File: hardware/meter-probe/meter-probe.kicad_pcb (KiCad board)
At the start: 2 copper layers, 38.9 x 74.1 mm, 19 parts, among them J1 Main Board, Q1 BSS138, SW1 Sensor Button, U1 RT9193, U2 TCS3472, U3 P82B96

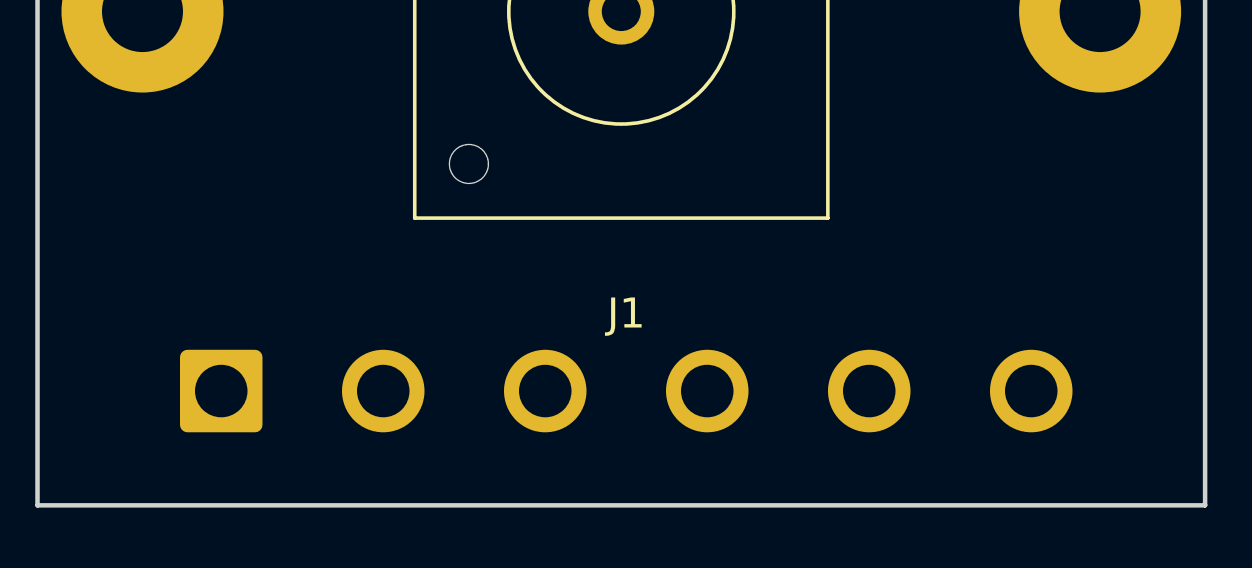
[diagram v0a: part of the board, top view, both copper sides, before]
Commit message: Updated wire connection footprint and PCB labeling
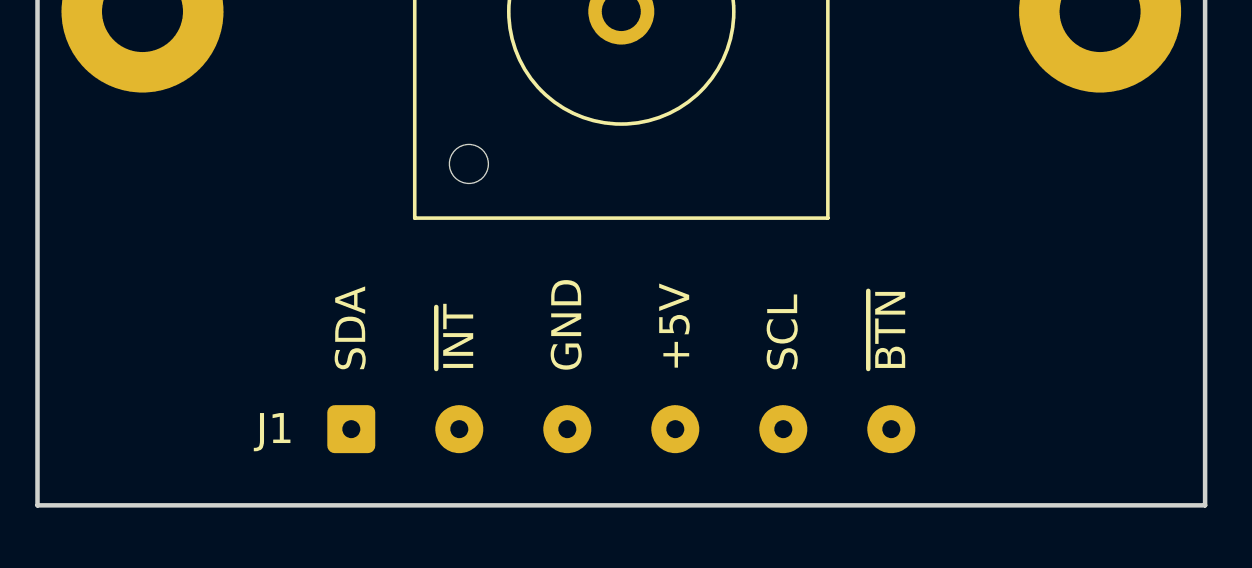
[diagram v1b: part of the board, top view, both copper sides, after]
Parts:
- J1: footprint Connector_Wire:SolderWire-1sqmm_1x06_P5.4mm_D1.4mm_OD2.7mm -> Connector_Wire:SolderWire-0.1sqmm_1x06_P3.6mm_D0.4mm_OD1mm
- moved J1 4.52 mm to (111.7, 130.8)
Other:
- board text added: "+5V"
- board text added: "GND"
- board text added: "SCL"
- board text added: "SDA"
- board text added: "~BTN"
- board text added: "~INT"

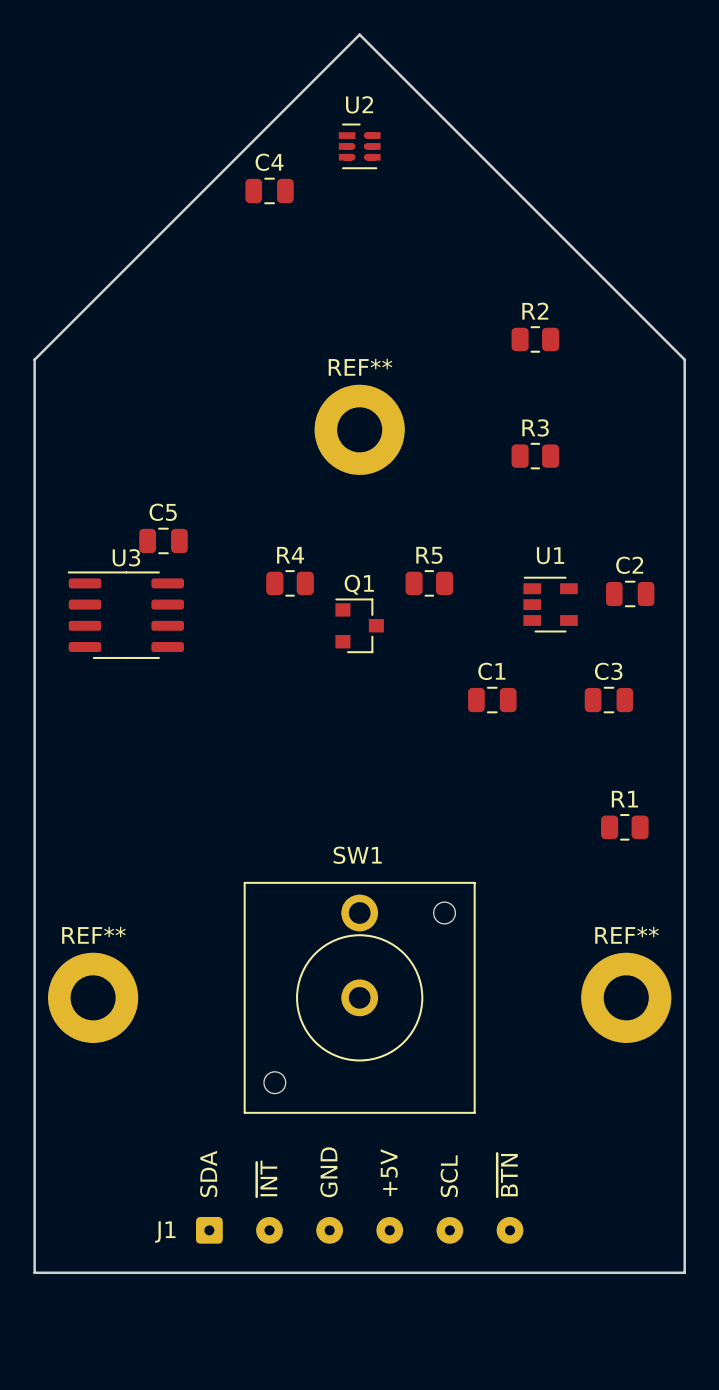
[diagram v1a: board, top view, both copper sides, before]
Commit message: Initial meter probe PCB layout
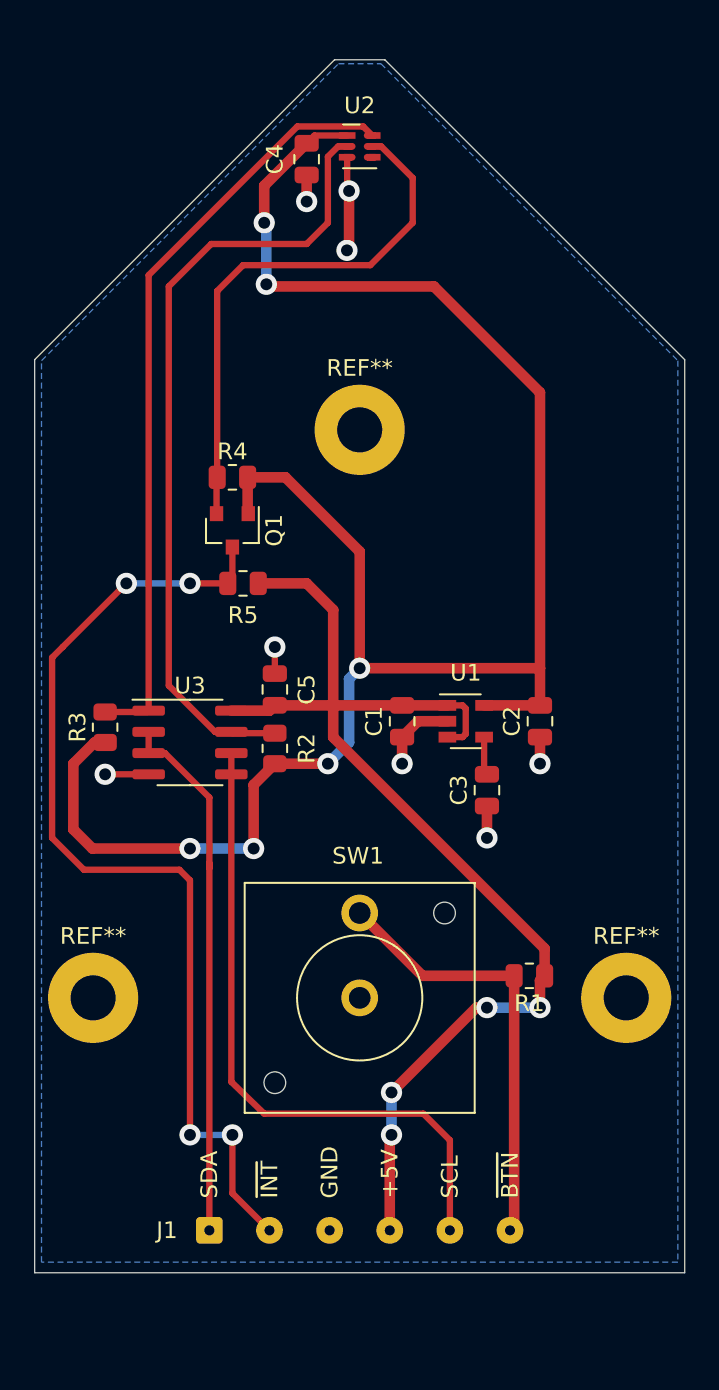
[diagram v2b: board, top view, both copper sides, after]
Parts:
- moved R3 30.4 mm to (105.4, 100.7), turned to 90 degrees
- moved R2 29.0 mm to (115.6, 102.0), turned to 90 degrees
- moved R5 11.2 mm to (113.7, 92.1), turned to 180 degrees
- moved C5 11.1 mm to (115.6, 98.4), turned to 90 degrees
- moved R1 10.6 mm to (130.8, 115.6), turned to 180 degrees
- moved Q1 9.52 mm to (113.0, 88.9), turned to 270 degrees
- moved C2 9.34 mm to (131.4, 100.3), turned to 90 degrees
- moved C3 9.08 mm to (128.3, 104.5), turned to 90 degrees
- moved U1 8.64 mm to (127.0, 100.3)
- moved U3 8.52 mm to (110.5, 101.6)
- moved R4 7.23 mm to (113.0, 85.7), turned to 180 degrees
- moved C1 5.55 mm to (123.2, 100.3), turned to 90 degrees
- moved C4 2.93 mm to (117.5, 66.7), turned to 270 degrees
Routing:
- net +3V3: track 0.00 -> 114.8 mm, vias 0 -> 6
- net +5V: track 0.00 -> 70.6 mm, vias 0 -> 4
- net /~INT: track 0.00 -> 59.2 mm, vias 0 -> 4
- net Net-(R2-Pad2): track 0.00 -> 47.9 mm
- net Net-(R3-Pad2): track 0.00 -> 46.0 mm
- net /SCL: track 0.00 -> 39.6 mm
- net Net-(Q1-Pad2): track 0.00 -> 32.6 mm
- net /SDA: track 0.00 -> 32.2 mm
- net /~BUTTON: track 0.00 -> 26.1 mm
- net GND: track 0.00 -> 19.7 mm, vias 0 -> 8
- net Net-(C3-Pad2): track 0.00 -> 2.30 mm
- added copper zone on B.Cu, net GND
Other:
- board size 38.9 x 74.1 mm -> 38.9 x 72.6 mm

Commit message: Updated PCB page properties
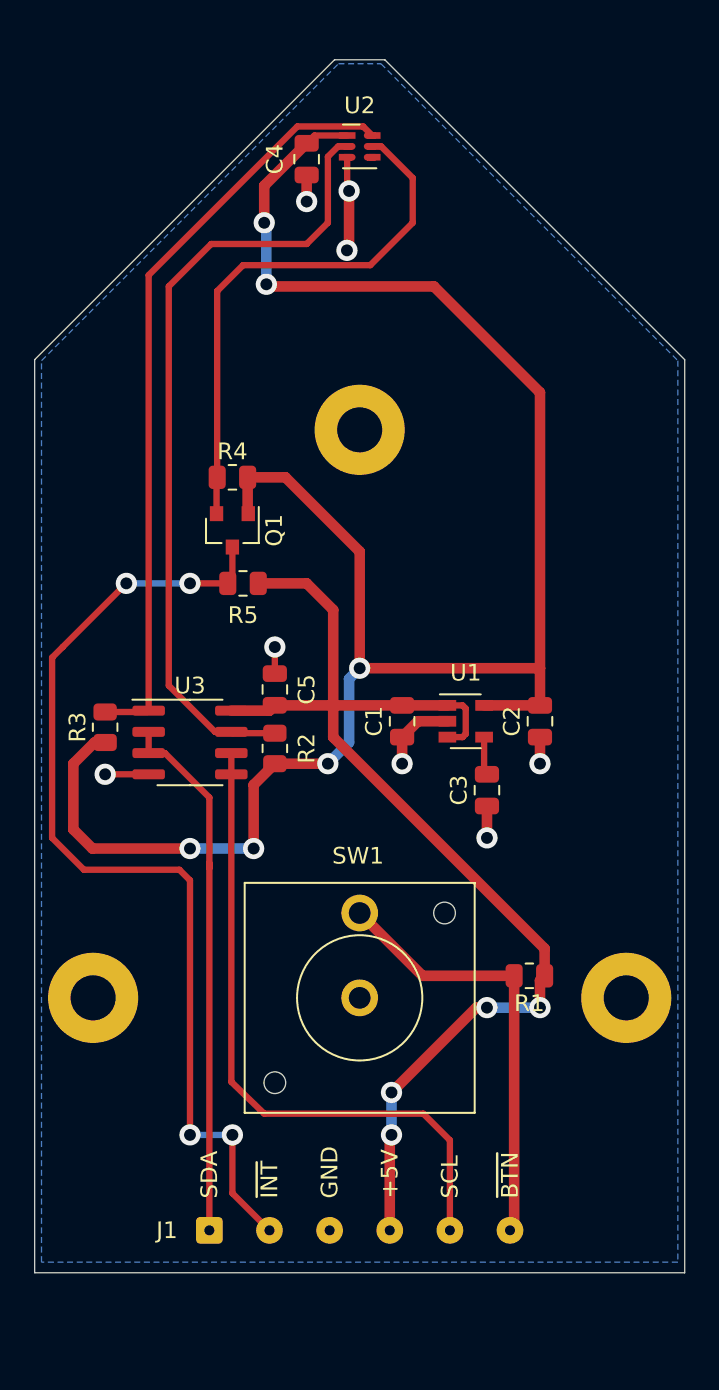
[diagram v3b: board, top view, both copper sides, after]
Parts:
- renumbered REF** to REF1, REF** to REF2, REF** to REF3

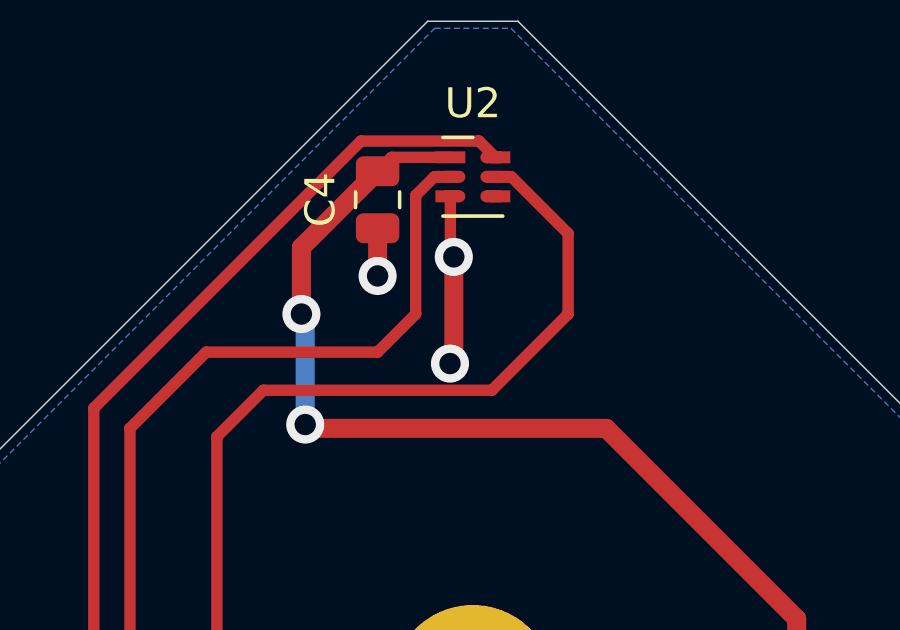
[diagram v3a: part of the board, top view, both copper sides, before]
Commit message: Added mounting holes to ground net
This required manually editing the kicad_pcb file, but it seems to work.
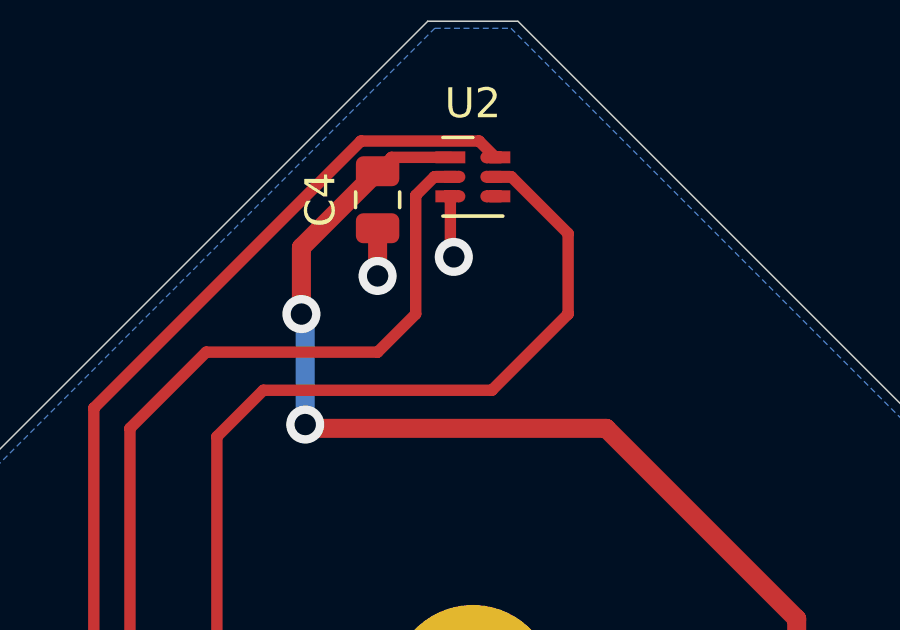
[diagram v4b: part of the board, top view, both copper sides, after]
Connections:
- REF1 pad 1: (no net) -> GND
- REF2 pad 1: (no net) -> GND
- REF3 pad 1: (no net) -> GND
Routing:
- net GND: track 19.7 -> 16.0 mm, vias 8 -> 7
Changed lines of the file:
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@@
     (thickness 1.6)
     (drawings 16)
-    (tracks 147)
+    (tracks 144)
     (zones 0)
     (modules 19)
@@
     (add_net "Net-(U2-Pad4)")
   )
+  (module MountingHole:MountingHole_2.7mm_M2.5_Pad locked (layer F.Cu)
+    (at 120.65 82.8816)
+    (descr "Mounting Hole 2.7mm, M2.5")
+    (tags "mounting hole 2.7mm m2.5")
+    (attr virtual)
+    (fp_text reference REF3 (at 0 -3.7) (layer F.SilkS) hide
+      (effects (font (size 1 1) (thickness 0.15)))
+    )
+    (fp_text value MountingHole_2.7mm_M2.5_Pad (at 0 3.7) (layer F.Fab) hide
+      (effects (font (size 1 1) (thickness 0.15)))
+    )
+    (fp_text user %R (at 0.3 0) (layer F.Fab)
+      (effects (font (size 1 1) (thickness 0.15)))
+    )
+    (fp_circle (center 0 0) (end 2.7 0) (layer Cmts.User) (width 0.15))
+    (fp_circle (center 0 0) (end 2.95 0) (layer F.CrtYd) (width 0.05))
+    (pad 1 thru_hole circle (at 0 0) (size 5.4 5.4) (drill 2.7) (layers *.Cu *.Mask)
+      (net 1 GND))
+  )
   (module Connector_Wire:SolderWire-0.1sqmm_1x06_P3.6mm_D0.4mm_OD1mm locked (layer F.Cu)
     (at 111.65 130.81)
@@
   )
   (module MountingHole:MountingHole_2.7mm_M2.5_Pad locked (layer F.Cu)
-    (at 120.65 82.8816)
-    (descr "Mounting Hole 2.7mm, M2.5")
-    (tags "mounting hole 2.7mm m2.5")
-    (attr virtual)
-    (fp_text reference REF3 (at 0 -3.7) (layer F.SilkS) hide
-      (effects (font (size 1 1) (thickness 0.15)))
-    )
-    (fp_text value MountingHole_2.7mm_M2.5_Pad (at 0 3.7) (layer F.Fab) hide
-      (effects (font (size 1 1) (thickness 0.15)))
-    )
-    (fp_circle (center 0 0) (end 2.7 0) (layer Cmts.User) (width 0.15))
-    (fp_circle (center 0 0) (end 2.95 0) (layer F.CrtYd) (width 0.05))
-    (fp_text user %R (at 0.3 0) (layer F.Fab)
-      (effects (font (size 1 1) (thickness 0.15)))
-    )
-    (pad 1 thru_hole circle (at 0 0) (size 5.4 5.4) (drill 2.7) (layers *.Cu *.Mask))
-  )
-  (module MountingHole:MountingHole_2.7mm_M2.5_Pad locked (layer F.Cu)
     (at 136.61 116.89)
     (descr "Mounting Hole 2.7mm, M2.5")
@@
       (effects (font (size 1 1) (thickness 0.15)))
     )
-    (pad 1 thru_hole circle (at 0 0) (size 5.4 5.4) (drill 2.7) (layers *.Cu *.Mask))
+    (pad 1 thru_hole circle (at 0 0) (size 5.4 5.4) (drill 2.7) (layers *.Cu *.Mask)
+      (net 1 GND))
   )
   (module MountingHole:MountingHole_2.7mm_M2.5_Pad locked (layer F.Cu)
@@
       (effects (font (size 1 1) (thickness 0.15)))
     )
-    (pad 1 thru_hole circle (at 0 0) (size 5.4 5.4) (drill 2.7) (layers *.Cu *.Mask))
+    (pad 1 thru_hole circle (at 0 0) (size 5.4 5.4) (drill 2.7) (layers *.Cu *.Mask)
+      (net 1 GND))
   )
   (module Capacitor_SMD:C_0805_2012Metric (layer F.Cu)
@@
   (segment (start 119.9 68.465) (end 120.015 68.58) (width 0.381) (layer F.Cu) (net 1))
   (segment (start 119.9 66.5608) (end 119.9 68.465) (width 0.381) (layer F.Cu) (net 1))
-  (via (at 119.888 72.136) (size 1.27) (drill 0.7112) (layers F.Cu B.Cu) (net 1))
-  (segment (start 120.015 72.009) (end 119.888 72.136) (width 0.635) (layer F.Cu) (net 1))
-  (segment (start 120.015 68.58) (end 120.015 72.009) (width 0.635) (layer F.Cu) (net 1))
   (segment (start 115.25 99.695) (end 115.57 99.375) (width 0.635) (layer F.Cu) (net 2))
   (segment (start 112.965 99.695) (end 115.25 99.695) (width 0.635) (layer F.Cu) (net 2))

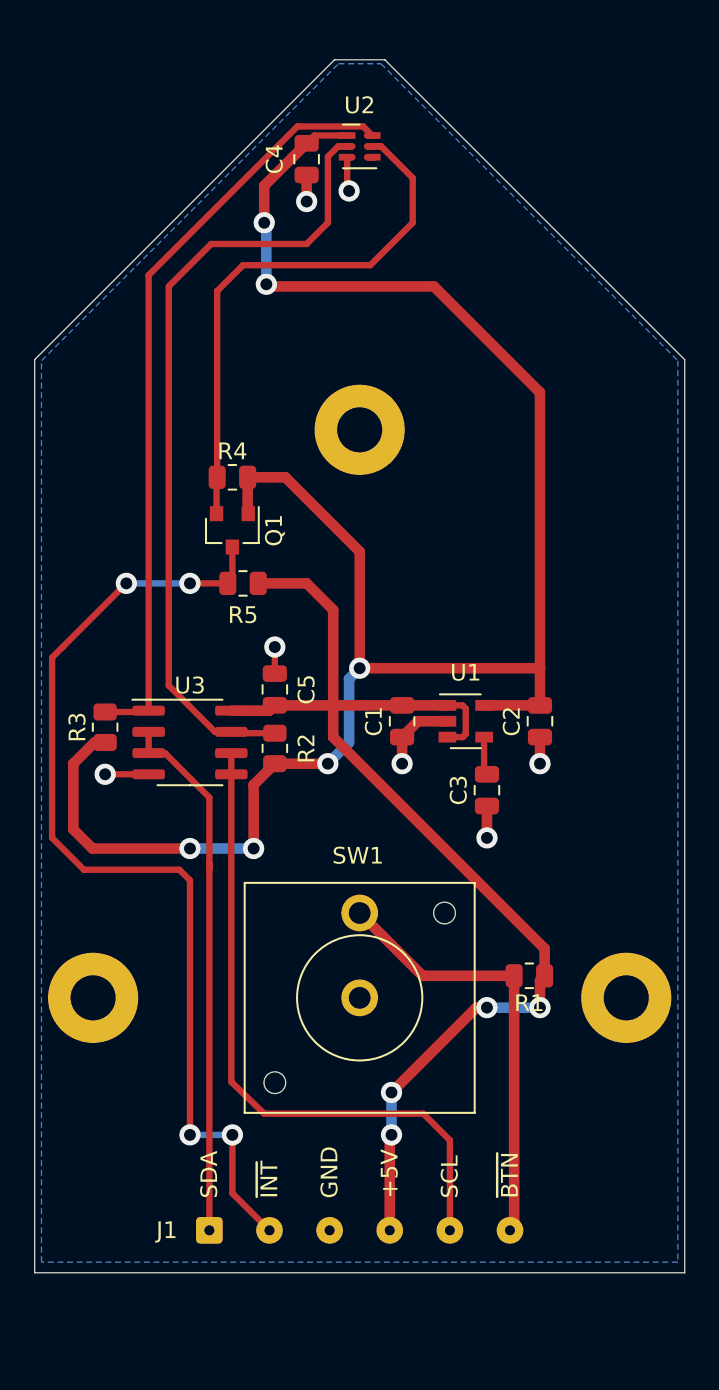
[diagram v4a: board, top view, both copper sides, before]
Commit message: Added silkscreen elements
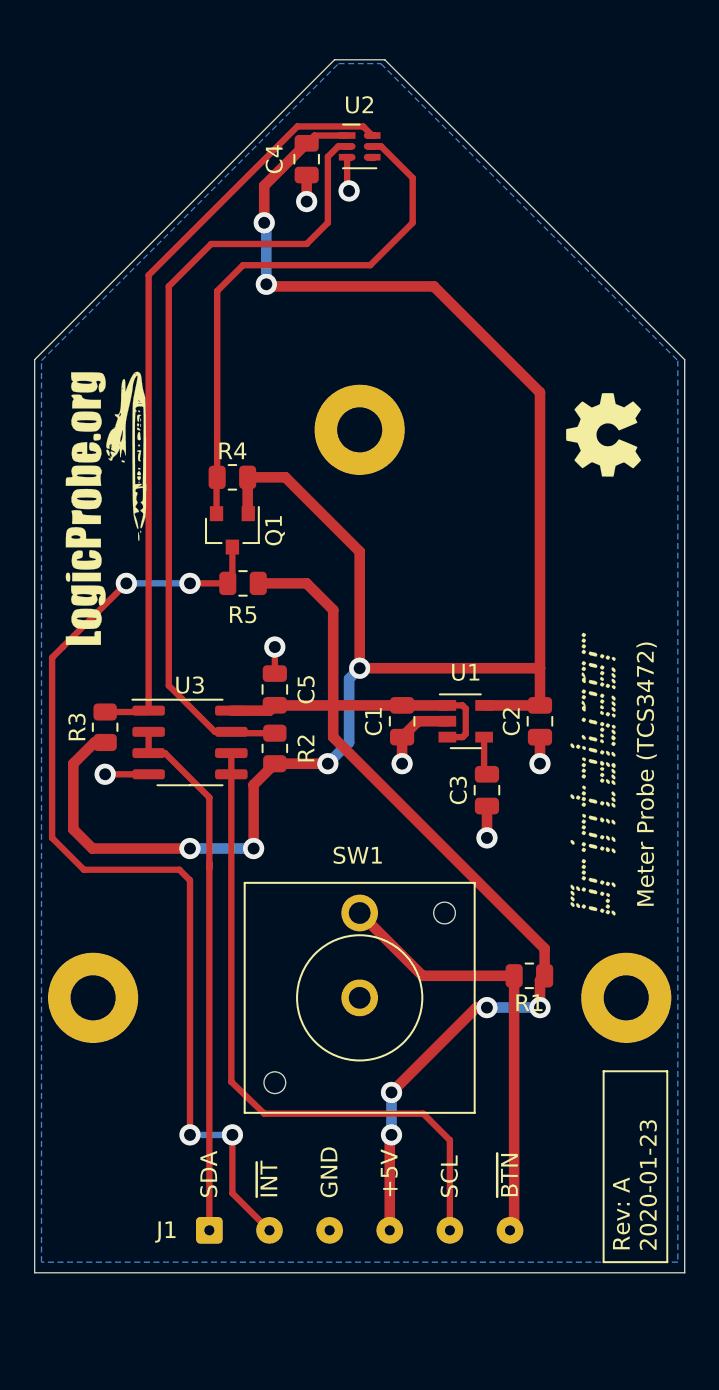
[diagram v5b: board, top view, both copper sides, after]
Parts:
- added G***: LOGO, lib_fp:LogicProbe, F.Cu at (105.4, 87.6)
- added G***: OSHW-logo_5mm, lib_fp:OSHW-logo_5mm, F.Cu at (135.3, 83.2)
- added G***: LOGO, lib_fp:Printalyzer-logo-16_9mm, F.Cu at (134.6, 103.5)
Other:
- board text added: "Meter Probe (TCS3472)"
- board text added: "Rev: A 2020-01-23"
